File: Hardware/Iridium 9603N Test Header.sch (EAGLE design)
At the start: 3 parts, among them J3 SS4-10-3.50-X-D

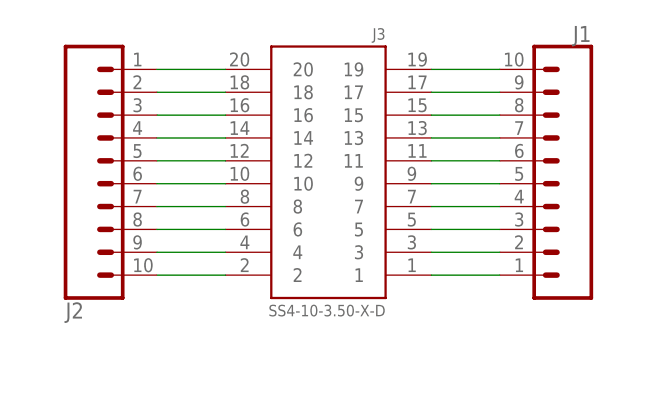
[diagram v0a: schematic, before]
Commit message: Added the dimensions
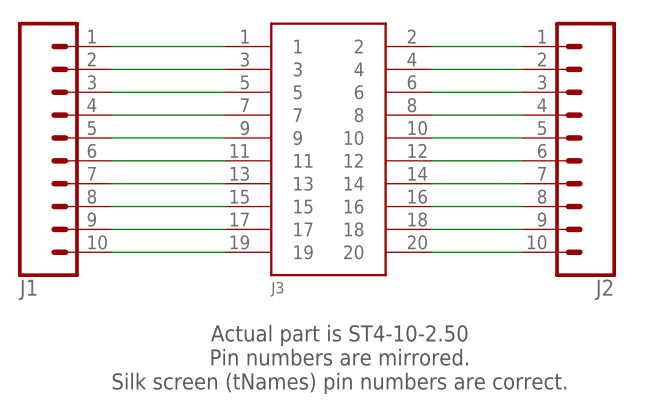
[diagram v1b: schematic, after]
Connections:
- net N$11: now also J2.10; no longer J2.1
- net N$12: now also J2.9; no longer J2.2
- net N$13: now also J2.8; no longer J2.3
- net N$14: now also J2.7; no longer J2.4
- net N$15: now also J2.6; no longer J2.5
- net N$16: now also J2.5; no longer J2.6
- net N$17: now also J2.4; no longer J2.7
- net N$18: now also J2.3; no longer J2.8
- net N$19: now also J2.2; no longer J2.9
- net N$20: now also J2.1; no longer J2.10
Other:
- note added: "Actual part is ST4-10-2.50 Pin numbers are mirrored. Silk screen (tNames) pin numbers are correct."
- moved on the sheet: J1, J2, J3
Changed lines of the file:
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@@
 <part name="FRAME1" library="frames" library_urn="urn:adsk.eagle:library:229" deviceset="A4L-LOC" device=""/>
 <part name="J1" library="SparkFun-Connectors" library_urn="urn:adsk.eagle:library:513" deviceset="CONN_10" device="&quot;" package3d_urn="urn:adsk.eagle:package:38157/1"/>
+<part name="J3" library="Iridium 9603N Test Header" deviceset="SS4-10-3.50-X-D" device=""/>
 <part name="J2" library="SparkFun-Connectors" library_urn="urn:adsk.eagle:library:513" deviceset="CONN_10" device="&quot;" package3d_urn="urn:adsk.eagle:package:38157/1"/>
-<part name="J3" library="Iridium 9603N Test Header" deviceset="SS4-10-3.50-X-D" device=""/>
 </parts>
 <sheets>
 <sheet>
 <plain>
+<text x="124.46" y="78.74" size="1.778" layer="97" align="bottom-center">Actual part is ST4-10-2.50
+Pin numbers are mirrored.
+Silk screen (tNames) pin numbers are correct.</text>
 </plain>
 <instances>
@@
 <attribute name="SHEET" x="230.505" y="5.08" size="2.54" layer="94"/>
 </instance>
-<instance part="J1" gate="G$1" x="152.4" y="109.22" smashed="yes" rot="MR0">
-<attribute name="VALUE" x="152.4" y="86.614" size="1.778" layer="96" font="vector" rot="MR0"/>
-<attribute name="NAME" x="152.4" y="117.348" size="1.778" layer="95" font="vector" rot="MR0"/>
+<instance part="J1" gate="G$1" x="88.9" y="99.06" smashed="yes" rot="MR180">
+<attribute name="VALUE" x="88.9" y="121.666" size="1.778" layer="96" font="vector" rot="MR180"/>
+<attribute name="NAME" x="88.9" y="90.932" size="1.778" layer="95" font="vector" rot="MR180"/>
 </instance>
-<instance part="J2" gate="G$1" x="93.98" y="96.52" smashed="yes" rot="MR180">
-<attribute name="VALUE" x="93.98" y="119.126" size="1.778" layer="96" font="vector" rot="MR180"/>
-<attribute name="NAME" x="93.98" y="88.392" size="1.778" layer="95" font="vector" rot="MR180"/>
+<instance part="J3" gate="G$1" x="111.76" y="116.84" smashed="yes">
+<attribute name="NAME" x="116.84" y="89.408" size="1.27" layer="95"/>
 </instance>
-<instance part="J3" gate="G$1" x="134.62" y="91.44" smashed="yes" rot="R180">
-<attribute name="NAME" x="129.54" y="118.872" size="1.27" layer="95" rot="R180"/>
-<attribute name="VALUE" x="129.54" y="88.138" size="1.27" layer="96" rot="R180"/>
+<instance part="J2" gate="G$1" x="154.94" y="99.06" smashed="yes" rot="R180">
+<attribute name="VALUE" x="154.94" y="121.666" size="1.778" layer="96" font="vector" rot="R180"/>
+<attribute name="NAME" x="154.94" y="90.932" size="1.778" layer="95" font="vector" rot="R180"/>
 </instance>
 </instances>
@@
 <pinref part="J3" gate="G$1" pin="1"/>
 <pinref part="J1" gate="G$1" pin="1"/>
-<wire x1="134.62" y1="91.44" x2="142.24" y2="91.44" width="0.1524" layer="91"/>
+<wire x1="111.76" y1="116.84" x2="99.06" y2="116.84" width="0.1524" layer="91"/>
 </segment>
 </net>
@@
 <pinref part="J3" gate="G$1" pin="3"/>
 <pinref part="J1" gate="G$1" pin="2"/>
-<wire x1="134.62" y1="93.98" x2="142.24" y2="93.98" width="0.1524" layer="91"/>
+<wire x1="111.76" y1="114.3" x2="99.06" y2="114.3" width="0.1524" layer="91"/>
 </segment>
 </net>
@@
 <pinref part="J3" gate="G$1" pin="5"/>
 <pinref part="J1" gate="G$1" pin="3"/>
-<wire x1="134.62" y1="96.52" x2="142.24" y2="96.52" width="0.1524" layer="91"/>
+<wire x1="111.76" y1="111.76" x2="99.06" y2="111.76" width="0.1524" layer="91"/>
 </segment>
 </net>
@@
 <pinref part="J3" gate="G$1" pin="7"/>
 <pinref part="J1" gate="G$1" pin="4"/>
-<wire x1="134.62" y1="99.06" x2="142.24" y2="99.06" width="0.1524" layer="91"/>
+<wire x1="111.76" y1="109.22" x2="99.06" y2="109.22" width="0.1524" layer="91"/>
 </segment>
 </net>
@@
 <pinref part="J3" gate="G$1" pin="9"/>
 <pinref part="J1" gate="G$1" pin="5"/>
-<wire x1="134.62" y1="101.6" x2="142.24" y2="101.6" width="0.1524" layer="91"/>
+<wire x1="111.76" y1="106.68" x2="99.06" y2="106.68" width="0.1524" layer="91"/>
 </segment>
 </net>
@@
 <pinref part="J3" gate="G$1" pin="11"/>
 <pinref part="J1" gate="G$1" pin="6"/>
-<wire x1="134.62" y1="104.14" x2="142.24" y2="104.14" width="0.1524" layer="91"/>
+<wire x1="111.76" y1="104.14" x2="99.06" y2="104.14" width="0.1524" layer="91"/>
 </segment>
 </net>
@@
 <pinref part="J3" gate="G$1" pin="13"/>
 <pinref part="J1" gate="G$1" pin="7"/>
-<wire x1="134.62" y1="106.68" x2="142.24" y2="106.68" width="0.1524" layer="91"/>
+<wire x1="111.76" y1="101.6" x2="99.06" y2="101.6" width="0.1524" layer="91"/>
 </segment>
 </net>
@@
 <pinref part="J3" gate="G$1" pin="15"/>
 <pinref part="J1" gate="G$1" pin="8"/>
-<wire x1="134.62" y1="109.22" x2="142.24" y2="109.22" width="0.1524" layer="91"/>
+<wire x1="111.76" y1="99.06" x2="99.06" y2="99.06" width="0.1524" layer="91"/>
 </segment>
 </net>
@@
 <pinref part="J3" gate="G$1" pin="17"/>
 <pinref part="J1" gate="G$1" pin="9"/>
-<wire x1="134.62" y1="111.76" x2="142.24" y2="111.76" width="0.1524" layer="91"/>
+<wire x1="111.76" y1="96.52" x2="99.06" y2="96.52" width="0.1524" layer="91"/>
 </segment>
 </net>
@@
 <pinref part="J3" gate="G$1" pin="19"/>
 <pinref part="J1" gate="G$1" pin="10"/>
-<wire x1="134.62" y1="114.3" x2="142.24" y2="114.3" width="0.1524" layer="91"/>
+<wire x1="111.76" y1="93.98" x2="99.06" y2="93.98" width="0.1524" layer="91"/>
 </segment>
 </net>
@@
 <segment>
 <pinref part="J3" gate="G$1" pin="20"/>
-<pinref part="J2" gate="G$1" pin="1"/>
-<wire x1="111.76" y1="114.3" x2="104.14" y2="114.3" width="0.1524" layer="91"/>
+<wire x1="134.62" y1="93.98" x2="144.78" y2="93.98" width="0.1524" layer="91"/>
+<pinref part="J2" gate="G$1" pin="10"/>
 </segment>
 </net>
@@
 <segment>
 <pinref part="J3" gate="G$1" pin="18"/>
-<pinref part="J2" gate="G$1" pin="2"/>
-<wire x1="111.76" y1="111.76" x2="104.14" y2="111.76" width="0.1524" layer="91"/>
+<wire x1="134.62" y1="96.52" x2="144.78" y2="96.52" width="0.1524" layer="91"/>
+<pinref part="J2" gate="G$1" pin="9"/>
 </segment>
 </net>
@@
 <segment>
 <pinref part="J3" gate="G$1" pin="16"/>
-<pinref part="J2" gate="G$1" pin="3"/>
-<wire x1="111.76" y1="109.22" x2="104.14" y2="109.22" width="0.1524" layer="91"/>
+<wire x1="134.62" y1="99.06" x2="144.78" y2="99.06" width="0.1524" layer="91"/>
+<pinref part="J2" gate="G$1" pin="8"/>
 </segment>
 </net>
@@
 <segment>
 <pinref part="J3" gate="G$1" pin="14"/>
-<pinref part="J2" gate="G$1" pin="4"/>
-<wire x1="111.76" y1="106.68" x2="104.14" y2="106.68" width="0.1524" layer="91"/>
+<wire x1="134.62" y1="101.6" x2="144.78" y2="101.6" width="0.1524" layer="91"/>
+<pinref part="J2" gate="G$1" pin="7"/>
 </segment>
 </net>
@@
 <segment>
 <pinref part="J3" gate="G$1" pin="12"/>
-<pinref part="J2" gate="G$1" pin="5"/>
-<wire x1="111.76" y1="104.14" x2="104.14" y2="104.14" width="0.1524" layer="91"/>
+<pinref part="J2" gate="G$1" pin="6"/>
+<wire x1="144.78" y1="104.14" x2="134.62" y2="104.14" width="0.1524" layer="91"/>
 </segment>
 </net>
@@
 <segment>
 <pinref part="J3" gate="G$1" pin="10"/>
-<pinref part="J2" gate="G$1" pin="6"/>
-<wire x1="111.76" y1="101.6" x2="104.14" y2="101.6" width="0.1524" layer="91"/>
+<pinref part="J2" gate="G$1" pin="5"/>
+<wire x1="144.78" y1="106.68" x2="134.62" y2="106.68" width="0.1524" layer="91"/>
 </segment>
 </net>
@@
 <segment>
 <pinref part="J3" gate="G$1" pin="8"/>
-<pinref part="J2" gate="G$1" pin="7"/>
-<wire x1="111.76" y1="99.06" x2="104.14" y2="99.06" width="0.1524" layer="91"/>
+<pinref part="J2" gate="G$1" pin="4"/>
+<wire x1="144.78" y1="109.22" x2="134.62" y2="109.22" width="0.1524" layer="91"/>
 </segment>
 </net>
@@
 <segment>
 <pinref part="J3" gate="G$1" pin="6"/>
-<pinref part="J2" gate="G$1" pin="8"/>
-<wire x1="111.76" y1="96.52" x2="104.14" y2="96.52" width="0.1524" layer="91"/>
+<pinref part="J2" gate="G$1" pin="3"/>
+<wire x1="144.78" y1="111.76" x2="134.62" y2="111.76" width="0.1524" layer="91"/>
 </segment>
 </net>
@@
 <segment>
 <pinref part="J3" gate="G$1" pin="4"/>
-<pinref part="J2" gate="G$1" pin="9"/>
-<wire x1="111.76" y1="93.98" x2="104.14" y2="93.98" width="0.1524" layer="91"/>
+<pinref part="J2" gate="G$1" pin="2"/>
+<wire x1="144.78" y1="114.3" x2="134.62" y2="114.3" width="0.1524" layer="91"/>
 </segment>
 </net>
@@
 <segment>
 <pinref part="J3" gate="G$1" pin="2"/>
-<pinref part="J2" gate="G$1" pin="10"/>
-<wire x1="111.76" y1="91.44" x2="104.14" y2="91.44" width="0.1524" layer="91"/>
+<pinref part="J2" gate="G$1" pin="1"/>
+<wire x1="144.78" y1="116.84" x2="134.62" y2="116.84" width="0.1524" layer="91"/>
 </segment>
 </net>
@@
 </drawing>
 <compatibility>
+<note version="6.3" minversion="6.2.2" severity="warning">
+Since Version 6.2.2 text objects can contain more than one line,
+which will not be processed correctly with this version.
+</note>
 <note version="8.2" severity="warning">
 Since Version 8.2, EAGLE supports online libraries. The ids

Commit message: Corrected the ST4-10-2.50 footprint
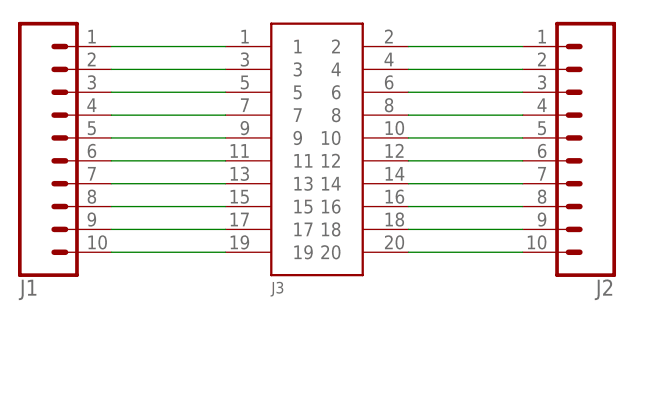
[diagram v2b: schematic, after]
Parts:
- J3: value SS4-10-3.50-X-D -> ST4-10-X.XX-X-D; device Iridium 9603N Test Header:SS4-10-3.50-X-D -> ST4-30-X.XX-X-D:ST4-10-X.XX-X-D
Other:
- note removed: "Actual part is ST4-10-2.50 Pin numbers are mirrored. Silk screen (tNames) pin numbers are correct."
- moved on the sheet: J3
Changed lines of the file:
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@@
 <part name="FRAME1" library="frames" library_urn="urn:adsk.eagle:library:229" deviceset="A4L-LOC" device=""/>
 <part name="J1" library="SparkFun-Connectors" library_urn="urn:adsk.eagle:library:513" deviceset="CONN_10" device="&quot;" package3d_urn="urn:adsk.eagle:package:38157/1"/>
-<part name="J3" library="Iridium 9603N Test Header" deviceset="SS4-10-3.50-X-D" device=""/>
+<part name="J3" library="ST4-30-X.XX-X-D" deviceset="ST4-10-X.XX-X-D" device=""/>
 <part name="J2" library="SparkFun-Connectors" library_urn="urn:adsk.eagle:library:513" deviceset="CONN_10" device="&quot;" package3d_urn="urn:adsk.eagle:package:38157/1"/>
 </parts>
@@
 <sheet>
 <plain>
-<text x="124.46" y="78.74" size="1.778" layer="97" align="bottom-center">Actual part is ST4-10-2.50
-Pin numbers are mirrored.
-Silk screen (tNames) pin numbers are correct.</text>
 </plain>
 <instances>
@@
 <net name="N$2" class="0">
 <segment>
+<pinref part="J3" gate="G$1" pin="2"/>
+<pinref part="J2" gate="G$1" pin="1"/>
+<wire x1="132.08" y1="116.84" x2="144.78" y2="116.84" width="0.1524" layer="91"/>
+</segment>
+</net>
+<net name="N$3" class="0">
+<segment>
 <pinref part="J3" gate="G$1" pin="3"/>
 <pinref part="J1" gate="G$1" pin="2"/>
@@
 </segment>
 </net>
-<net name="N$3" class="0">
+<net name="N$4" class="0">
+<segment>
+<pinref part="J3" gate="G$1" pin="4"/>
+<pinref part="J2" gate="G$1" pin="2"/>
+<wire x1="132.08" y1="114.3" x2="144.78" y2="114.3" width="0.1524" layer="91"/>
+</segment>
+</net>
+<net name="N$5" class="0">
 <segment>
 <pinref part="J3" gate="G$1" pin="5"/>
@@
 </segment>
 </net>
-<net name="N$4" class="0">
+<net name="N$6" class="0">
+<segment>
+<pinref part="J3" gate="G$1" pin="6"/>
+<pinref part="J2" gate="G$1" pin="3"/>
+<wire x1="132.08" y1="111.76" x2="144.78" y2="111.76" width="0.1524" layer="91"/>
+</segment>
+</net>
+<net name="N$7" class="0">
 <segment>
 <pinref part="J3" gate="G$1" pin="7"/>
@@
 </segment>
 </net>
-<net name="N$5" class="0">
+<net name="N$8" class="0">
+<segment>
+<pinref part="J3" gate="G$1" pin="8"/>
+<pinref part="J2" gate="G$1" pin="4"/>
+<wire x1="132.08" y1="109.22" x2="144.78" y2="109.22" width="0.1524" layer="91"/>
+</segment>
+</net>
+<net name="N$9" class="0">
 <segment>
 <pinref part="J3" gate="G$1" pin="9"/>
@@
 </segment>
 </net>
-<net name="N$6" class="0">
+<net name="N$10" class="0">
+<segment>
+<pinref part="J3" gate="G$1" pin="10"/>
+<pinref part="J2" gate="G$1" pin="5"/>
+<wire x1="132.08" y1="106.68" x2="144.78" y2="106.68" width="0.1524" layer="91"/>
+</segment>
+</net>
+<net name="N$11" class="0">
 <segment>
 <pinref part="J3" gate="G$1" pin="11"/>
@@
 </segment>
 </net>
-<net name="N$7" class="0">
+<net name="N$12" class="0">
+<segment>
+<pinref part="J3" gate="G$1" pin="12"/>
+<pinref part="J2" gate="G$1" pin="6"/>
+<wire x1="132.08" y1="104.14" x2="144.78" y2="104.14" width="0.1524" layer="91"/>
+</segment>
+</net>
+<net name="N$13" class="0">
 <segment>
 <pinref part="J3" gate="G$1" pin="13"/>
@@
 </segment>
 </net>
-<net name="N$8" class="0">
+<net name="N$14" class="0">
+<segment>
+<pinref part="J3" gate="G$1" pin="14"/>
+<pinref part="J2" gate="G$1" pin="7"/>
+<wire x1="132.08" y1="101.6" x2="144.78" y2="101.6" width="0.1524" layer="91"/>
+</segment>
+</net>
+<net name="N$15" class="0">
 <segment>
 <pinref part="J3" gate="G$1" pin="15"/>
@@
 </segment>
 </net>
-<net name="N$9" class="0">
+<net name="N$16" class="0">
+<segment>
+<pinref part="J3" gate="G$1" pin="16"/>
+<pinref part="J2" gate="G$1" pin="8"/>
+<wire x1="132.08" y1="99.06" x2="144.78" y2="99.06" width="0.1524" layer="91"/>
+</segment>
+</net>
+<net name="N$17" class="0">
 <segment>
 <pinref part="J3" gate="G$1" pin="17"/>
@@
 </segment>
 </net>
-<net name="N$10" class="0">
+<net name="N$18" class="0">
+<segment>
+<pinref part="J3" gate="G$1" pin="18"/>
+<pinref part="J2" gate="G$1" pin="9"/>
+<wire x1="132.08" y1="96.52" x2="144.78" y2="96.52" width="0.1524" layer="91"/>
+</segment>
+</net>
+<net name="N$19" class="0">
 <segment>
 <pinref part="J3" gate="G$1" pin="19"/>
@@
 </segment>
 </net>
-<net name="N$11" class="0">
+<net name="N$20" class="0">
 <segment>
 <pinref part="J3" gate="G$1" pin="20"/>
-<wire x1="134.62" y1="93.98" x2="144.78" y2="93.98" width="0.1524" layer="91"/>
 <pinref part="J2" gate="G$1" pin="10"/>
-</segment>
-</net>
-<net name="N$12" class="0">
-<segment>
-<pinref part="J3" gate="G$1" pin="18"/>
-<wire x1="134.62" y1="96.52" x2="144.78" y2="96.52" width="0.1524" layer="91"/>
-<pinref part="J2" gate="G$1" pin="9"/>
-</segment>
-</net>
-<net name="N$13" class="0">
-<segment>
-<pinref part="J3" gate="G$1" pin="16"/>
-<wire x1="134.62" y1="99.06" x2="144.78" y2="99.06" width="0.1524" layer="91"/>
-<pinref part="J2" gate="G$1" pin="8"/>
-</segment>
-</net>
-<net name="N$14" class="0">
-<segment>
-<pinref part="J3" gate="G$1" pin="14"/>
-<wire x1="134.62" y1="101.6" x2="144.78" y2="101.6" width="0.1524" layer="91"/>
-<pinref part="J2" gate="G$1" pin="7"/>
-</segment>
-</net>
-<net name="N$15" class="0">
-<segment>
-<pinref part="J3" gate="G$1" pin="12"/>
-<pinref part="J2" gate="G$1" pin="6"/>
-<wire x1="144.78" y1="104.14" x2="134.62" y2="104.14" width="0.1524" layer="91"/>
-</segment>
-</net>
-<net name="N$16" class="0">
-<segment>
-<pinref part="J3" gate="G$1" pin="10"/>
-<pinref part="J2" gate="G$1" pin="5"/>
-<wire x1="144.78" y1="106.68" x2="134.62" y2="106.68" width="0.1524" layer="91"/>
-</segment>
-</net>
-<net name="N$17" class="0">
-<segment>
-<pinref part="J3" gate="G$1" pin="8"/>
-<pinref part="J2" gate="G$1" pin="4"/>
-<wire x1="144.78" y1="109.22" x2="134.62" y2="109.22" width="0.1524" layer="91"/>
-</segment>
-</net>
-<net name="N$18" class="0">
-<segment>
-<pinref part="J3" gate="G$1" pin="6"/>
-<pinref part="J2" gate="G$1" pin="3"/>
-<wire x1="144.78" y1="111.76" x2="134.62" y2="111.76" width="0.1524" layer="91"/>
-</segment>
-</net>
-<net name="N$19" class="0">
-<segment>
-<pinref part="J3" gate="G$1" pin="4"/>
-<pinref part="J2" gate="G$1" pin="2"/>
-<wire x1="144.78" y1="114.3" x2="134.62" y2="114.3" width="0.1524" layer="91"/>
-</segment>
-</net>
-<net name="N$20" class="0">
-<segment>
-<pinref part="J3" gate="G$1" pin="2"/>
-<pinref part="J2" gate="G$1" pin="1"/>
-<wire x1="144.78" y1="116.84" x2="134.62" y2="116.84" width="0.1524" layer="91"/>
+<wire x1="132.08" y1="93.98" x2="144.78" y2="93.98" width="0.1524" layer="91"/>
 </segment>
 </net>
@@
 </drawing>
 <compatibility>
-<note version="6.3" minversion="6.2.2" severity="warning">
-Since Version 6.2.2 text objects can contain more than one line,
-which will not be processed correctly with this version.
-</note>
 <note version="8.2" severity="warning">
 Since Version 8.2, EAGLE supports online libraries. The ids
